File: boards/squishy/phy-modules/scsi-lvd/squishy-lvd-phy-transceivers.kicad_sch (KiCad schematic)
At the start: 150 parts, among them Q1 PMDPB58UPE,115, Q2 PMDPB58UPE,115, Q3 PMDPB58UPE,115, Q4 PMDPB58UPE,115, U10 SN65LVDS180-Q1, U11 SN65LVDS180-Q1, U12 FIN1027A, U13 SN65LVDS180-Q1, U14 SN65LVDS180-Q1, U15 FIN1027A, U16 SN65LVDS180-Q1, U17 SN65LVDS180-Q1, U18 FIN1027A, U19 SN65LVDS180-Q1, U2 SN65LVDS180-Q1, U20 SN65LVDS180-Q1, U22 SN65LVDS180-Q1, U23 SN65LVDS180-Q1, U24 FIN1027A, U25 SN65LVDS180-Q1, U26 SN65LVDS180-Q1, U27 SN65LVDS180-Q1, U28 SN65LVDS180-Q1, U29 SN65LVDS180-Q1, U3 FIN1027A, U30 SN65LVDS180-Q1, U31 SN65LVDS180-Q1, U34 FIN1027A, U35 FIN1027A, U36 FIN1027A, U37 FIN1027A, U4 SN65LVDS180-Q1, U42 SN65LVDS180-Q1, U43 SN65LVDS180-Q1, U44 SN65LVDS180-Q1, U45 SN65LVDS180-Q1, U47 SN65LVDS180-Q1, U5 SN65LVDS180-Q1, U6 FIN1027A, U7 SN65LVDS180-Q1, U8 SN65LVDS180-Q1, U9 FIN1027A

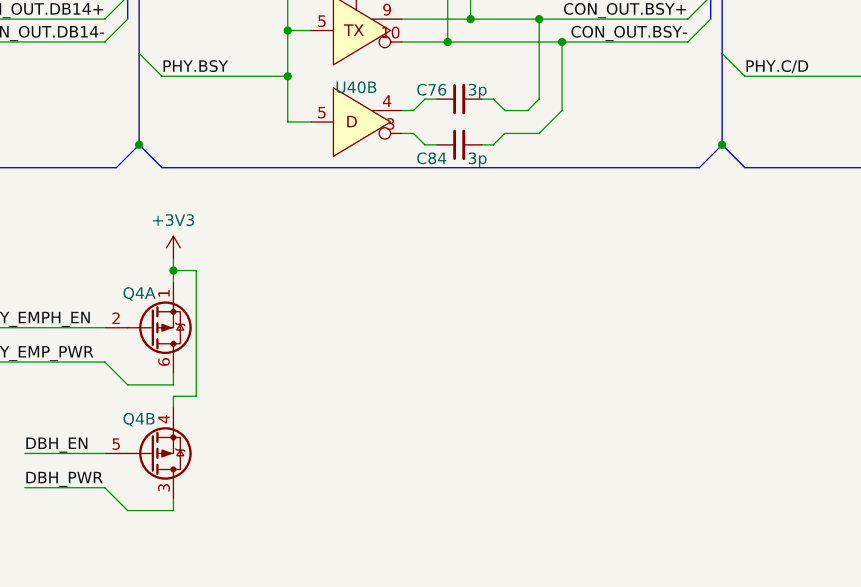
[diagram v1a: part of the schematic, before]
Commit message: squishy: phy: Added pull-downs on the LVD PHY enables to ensure output bus is High-Z on power up
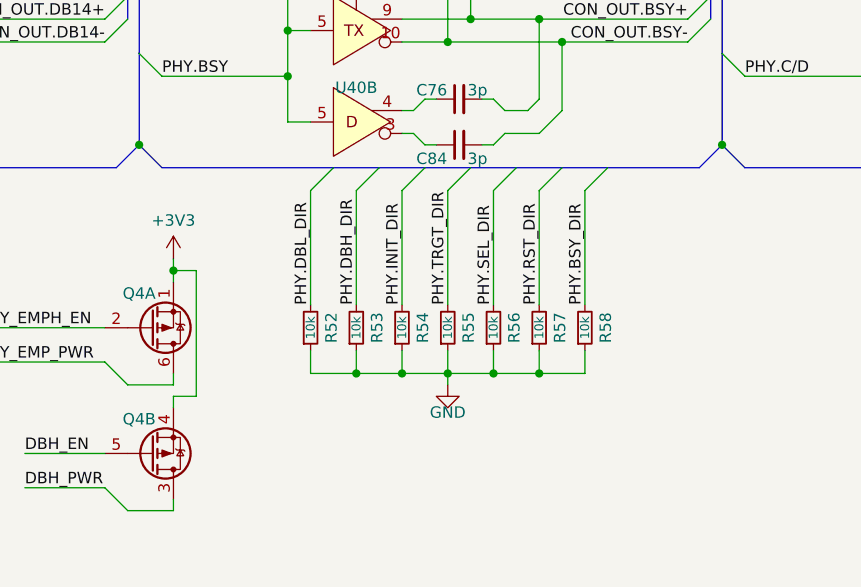
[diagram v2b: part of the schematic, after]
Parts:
- added R52, R53, R54, R55, R56, R57, R58: 10k, rhais_rcl:R0603, symbol Device:R_Small
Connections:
- net GND: now also R52.1, R53.1, R54.1, R55.1, R56.1, R57.1, R58.1
- net PHY.BSY_DIR: now also R58.2
- net PHY.DBH_DIR: now also R53.2
- net PHY.DBL_DIR: now also R52.2
- net PHY.INIT_DIR: now also R54.2
- net PHY.RST_DIR: now also R57.2
- net PHY.SEL_DIR: now also R56.2
- net PHY.TRGT_DIR: now also R55.2

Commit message: squishy:  phy: lvd: Upgraded to KiCad v9
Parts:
- R52, R53, R54, R55, R56, R57, R58: footprint rhais_rcl:R0603 -> rhais_rcl:R0402
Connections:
- net DB7E-: now reaches C12.1, U24.7
- net DB13E+: now reaches C59.1, U15.8
- net ACKE-: now reaches C45.1, U36.7
- net ACKE+: now reaches C44.1, U36.8
- net DB8E-: now reaches C66.1, U34.5
- net C/DE-: now reaches C85.1, U37.7
- net C/DE+: now reaches C77.1, U37.8
- net RSTE-: now reaches C47.1, U49.3
- net RSTE+: now reaches C46.1, U49.4
- net DP1E-: now reaches C26.1, U46.3
- net DP1E+: now reaches C25.1, U46.4
- net ATNE-: now reaches C68.1, U36.5
- net ATNE+: now reaches C60.1, U36.6
- net DB9E-: now reaches C82.1, U34.7
- net DB14E-: now reaches C83.1, U12.7
- net DB14E+: now reaches C75.1, U12.8
- net DB11E+: now reaches C32.1, U35.8
- net DB6E-: now reaches C19.1, U24.5
- net DB3E-: now reaches C52.1, U6.7
- net REQE+: now reaches C63.1, U18.8
- net I/OE+: now reaches C79.1, U18.6
- net REQE-: now reaches C71.1, U18.7
- net DB10E+: now reaches C30.1, U35.6
- net I/OE-: now reaches C87.1, U18.5
- net BSYE+: now reaches C76.1, U40.4
- net DB10E-: now reaches C31.1, U35.5
- net DB8E+: now reaches C58.1, U34.6
- net DB15E-: now reaches C38.1, U12.5
- net DB15E+: now reaches C37.1, U12.6
- net DB2E+: now reaches C9.1, U6.6
- net DB9E+: now reaches C74.1, U34.8
- net DB12E+: now reaches C23.1, U15.6
- net MSGE-: now reaches C70.1, U37.5
- net MSGE+: now reaches C62.1, U37.6
- net DB0E+: now reaches C2.1, U3.6
- net BSYE-: now reaches C84.1, U40.3
- net DB13E-: now reaches C67.1, U15.7
- net DB2E-: now reaches C10.1, U6.5
- net DB4E-: now reaches C54.1, U9.5
- net DB12E-: now reaches C24.1, U15.5
- net DB11E-: now reaches C33.1, U35.7
- net SELE-: now reaches C69.1, U41.3
- net SELE+: now reaches C61.1, U41.4
- net DB5E-: now reaches C17.1, U9.7
- net DB3E+: now reaches C51.1, U6.8
- net DB7E+: now reaches C11.1, U24.8
- net DB4E+: now reaches C53.1, U9.6
- net DB5E+: now reaches C16.1, U9.8
- net DB0E-: now reaches C3.1, U3.5
- net DB1E-: now reaches C5.1, U3.7
- net DB1E+: now reaches C4.1, U3.8
- net DP0E+: now reaches C39.1, U48.4
- net DB6E+: now reaches C18.1, U24.6
- net DP0E-: now reaches C40.1, U48.3
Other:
- moved on the sheet: C106, C107, C108, C109, C110, C111, C15, C22, C43, C50, C57, C72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
